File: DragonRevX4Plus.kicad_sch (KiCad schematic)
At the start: 14 parts, among them J14 PWR_LED, J15 PWR_SWITCH, J7 COMPOSITE

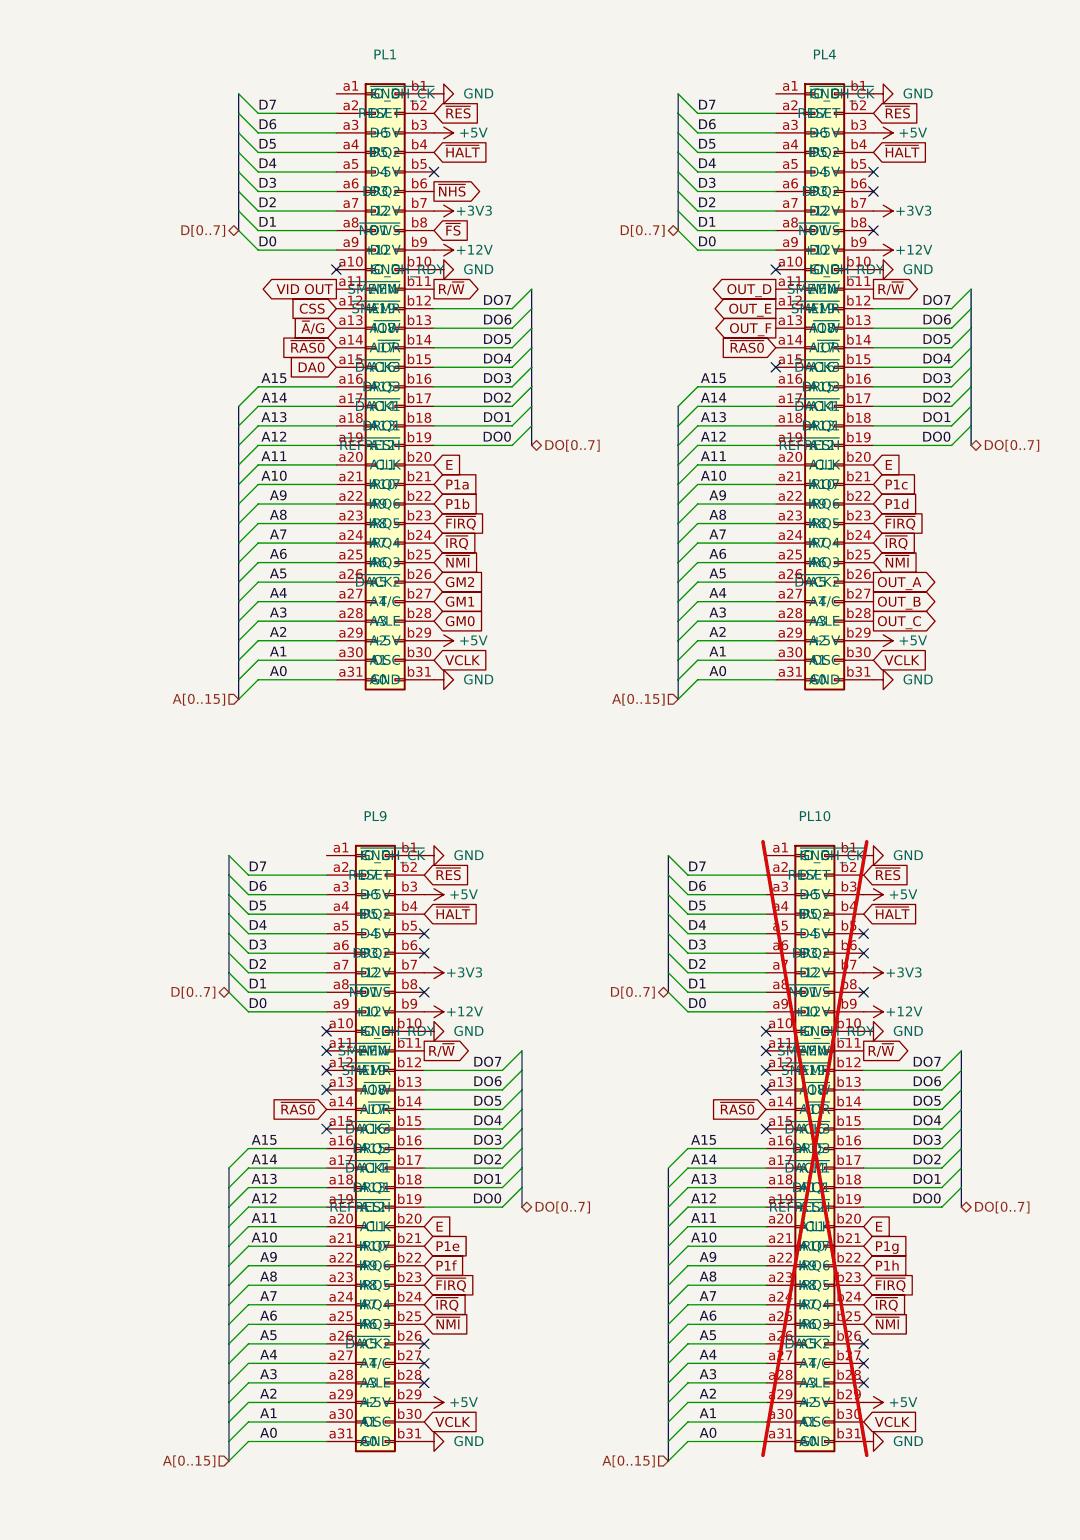
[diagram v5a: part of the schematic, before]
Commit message: Migrate to plugin memory module
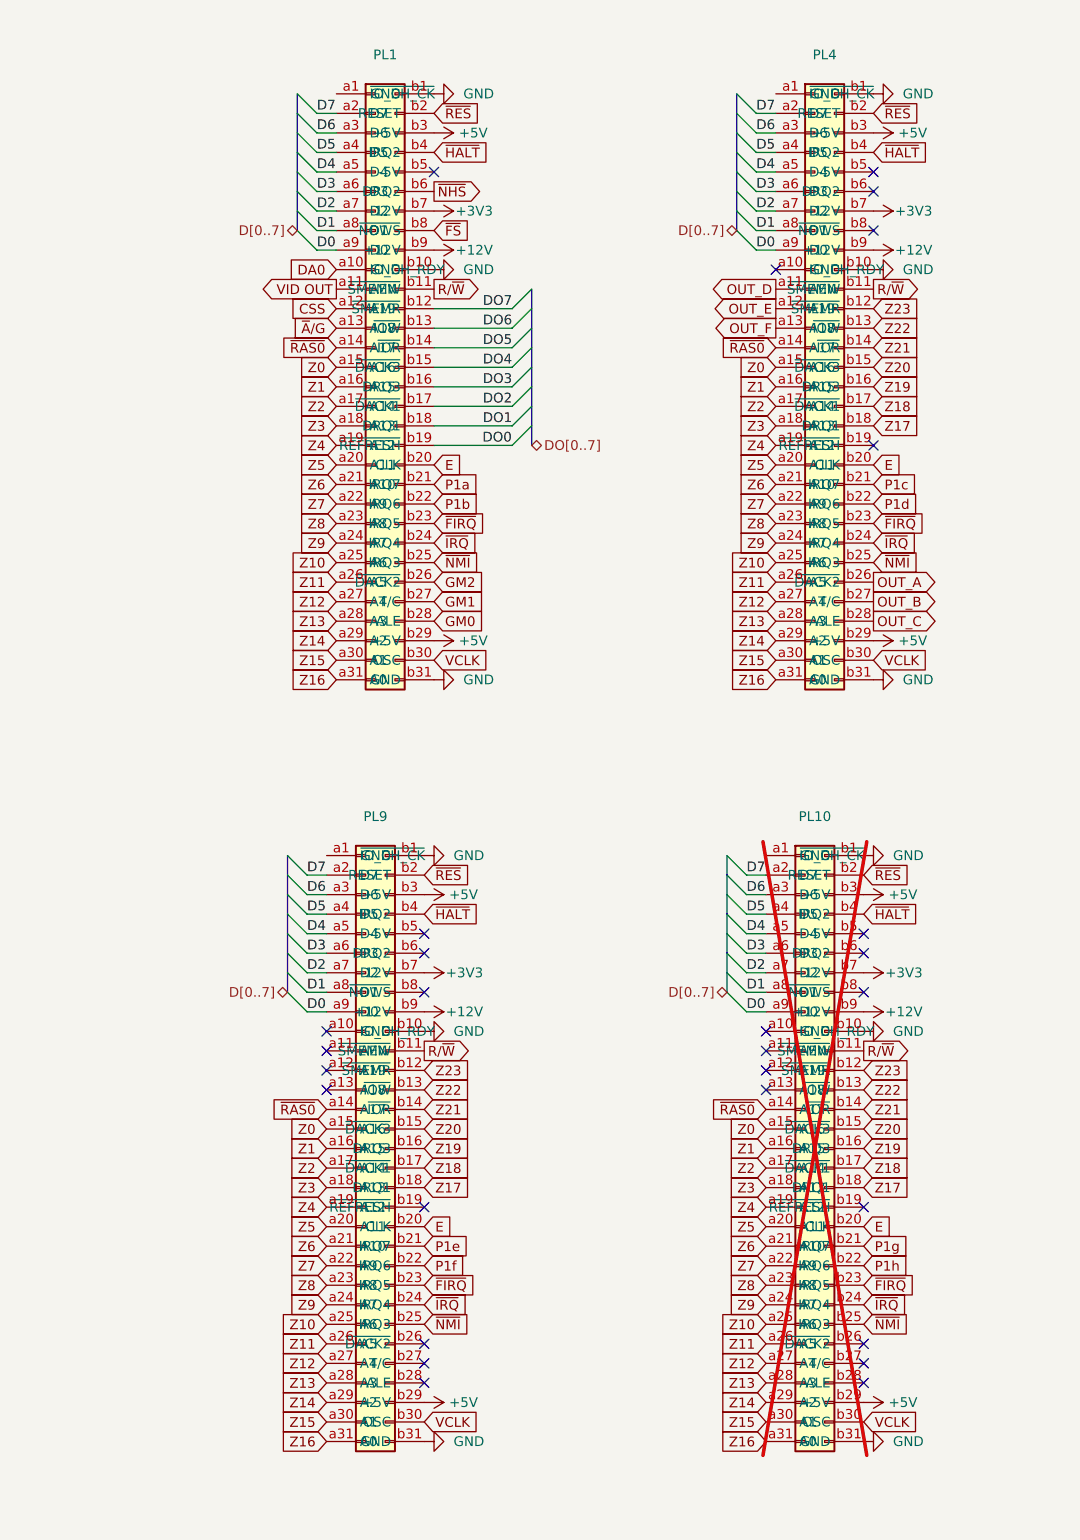
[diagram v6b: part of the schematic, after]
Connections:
- net DA0: now also PL1.a10 (IO_CH_RDY); no longer PL1.a15 (A16)
- net DO0: no longer PL10.b19 (~{REFRESH}), PL4.b19 (~{REFRESH}), PL9.b19 (~{REFRESH})
- net DO1: no longer PL10.b18 (DRQ1), PL4.b18 (DRQ1), PL9.b18 (DRQ1)
- net DO2: no longer PL10.b17 (~{DACK1}), PL4.b17 (~{DACK1}), PL9.b17 (~{DACK1})
- net DO3: no longer PL10.b16 (DRQ3), PL4.b16 (DRQ3), PL9.b16 (DRQ3)
- net DO4: no longer PL10.b15 (~{DACK3}), PL4.b15 (~{DACK3}), PL9.b15 (~{DACK3})
- net DO5: no longer PL10.b14 (~{IOR}), PL4.b14 (~{IOR}), PL9.b14 (~{IOR})
- net DO6: no longer PL10.b13 (~{IOW}), PL4.b13 (~{IOW}), PL9.b13 (~{IOW})
- net DO7: no longer PL10.b12 (~{SMEMR}), PL4.b12 (~{SMEMR}), PL9.b12 (~{SMEMR})
- net Z0: now reaches PL10.a15 (A16)
- net Z0: now also PL1.a15 (A16), PL4.a15 (A16), PL9.a15 (A16)
- net A0 renamed Z16
- net A1 renamed Z15
- net A10 renamed Z6
- net A11 renamed Z5
- net A12 renamed Z4
- net A13 renamed Z3
- net A14 renamed Z2
- net A15 renamed Z1
- net A2 renamed Z14
- net A3 renamed Z13
- net A4 renamed Z12
- net A5 renamed Z11
- net A6 renamed Z10
- net A7 renamed Z9
- net A8 renamed Z8
- net A9 renamed Z7
- new net Z17: PL10.b18 (DRQ1), PL4.b18 (DRQ1), PL9.b18 (DRQ1)
- new net Z18: PL10.b17 (~{DACK1}), PL4.b17 (~{DACK1}), PL9.b17 (~{DACK1})
- new net Z19: PL10.b16 (DRQ3), PL4.b16 (DRQ3), PL9.b16 (DRQ3)
- new net Z20: PL10.b15 (~{DACK3}), PL4.b15 (~{DACK3}), PL9.b15 (~{DACK3})
- new net Z21: PL10.b14 (~{IOR}), PL4.b14 (~{IOR}), PL9.b14 (~{IOR})
- new net Z22: PL10.b13 (~{IOW}), PL4.b13 (~{IOW}), PL9.b13 (~{IOW})
- new net Z23: PL10.b12 (~{SMEMR}), PL4.b12 (~{SMEMR}), PL9.b12 (~{SMEMR})
- no-connect marks 32 -> 31

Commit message: progress routing
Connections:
- net VID OUT: now also PL1.a1 (~{IO_CH_CK}); no longer PL1.a11 (AEN)
- net SOUNDL renamed OUT_L
- net SOUNDR renamed OUT_R
- no-connect marks 31 -> 32
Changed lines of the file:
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@@
 	)
 	(no_connect
+		(at 304.8 50.8)
+	)
+	(no_connect
 		(at 373.38 134.62)
 	)
@@
 		)
 	)
+	(global_label "VID OUT"
+		(shape output)
+		(at 304.8 25.4 180)
+		(fields_autoplaced yes)
+		(effects
+			(font
+				(size 1.27 1.27)
+			)
+			(justify right)
+		)
+		(property "Intersheetrefs" "${INTERSHEET_REFS}"
+			(at 294.2552 25.4 0)
+			(effects
+				(font
+					(size 1.27 1.27)
+				)
+				(justify right)
+				(hide yes)
+			)
+		)
+	)
 	(global_label "Z11"
 		(shape input)
@@
 		)
 	)
+	(global_label "OUT_R"
+		(shape input)
+		(at 78.74 60.96 0)
+		(fields_autoplaced yes)
+		(effects
+			(font
+				(size 1.27 1.27)
+			)
+			(justify left)
+		)
+		(property "Intersheetrefs" "${INTERSHEET_REFS}"
+			(at 87.5914 60.96 0)
+			(effects
+				(font
+					(size 1.27 1.27)
+				)
+				(justify left)
+				(hide yes)
+			)
+		)
+	)
 	(global_label "~{NMI}"
 		(shape input)
@@
 		)
 	)
-	(global_label "VID OUT"
-		(shape output)
-		(at 304.8 50.8 180)
-		(fields_autoplaced yes)
-		(effects
-			(font
-				(size 1.27 1.27)
-			)
-			(justify right)
-		)
-		(property "Intersheetrefs" "${INTERSHEET_REFS}"
-			(at 294.2552 50.8 0)
-			(effects
-				(font
-					(size 1.27 1.27)
-				)
-				(justify right)
-				(hide yes)
-			)
-		)
-	)
 	(global_label "Z10"
 		(shape input)
@@
 		)
 	)
-	(global_label "SOUNDL"
-		(shape input)
-		(at 78.74 58.42 0)
-		(fields_autoplaced yes)
-		(effects
-			(font
-				(size 1.27 1.27)
-			)
-			(justify left)
-		)
-		(property "Intersheetrefs" "${INTERSHEET_REFS}"
-			(at 89.2243 58.42 0)
-			(effects
-				(font
-					(size 1.27 1.27)
-				)
-				(justify left)
-				(hide yes)
-			)
-		)
-	)
 	(global_label "Z2"
 		(shape input)
@@
 		)
 	)
+	(global_label "OUT_L"
+		(shape input)
+		(at 78.74 58.42 0)
+		(fields_autoplaced yes)
+		(effects
+			(font
+				(size 1.27 1.27)
+			)
+			(justify left)
+		)
+		(property "Intersheetrefs" "${INTERSHEET_REFS}"
+			(at 87.3495 58.42 0)
+			(effects
+				(font
+					(size 1.27 1.27)
+				)
+				(justify left)
+				(hide yes)
+			)
+		)
+	)
 	(global_label "Z16"
 		(shape input)
@@
 				(hide yes)
 			)
-		)
-	)
-	(global_label "SOUNDR"
-		(shape input)
-		(at 78.74 60.96 0)
-		(fields_autoplaced yes)
-		(effects
-			(font
-				(size 1.27 1.27)
-			)
-			(justify left)
-		)
-		(property "Intersheetrefs" "${INTERSHEET_REFS}"
-			(at 89.4662 60.96 0)
-			(effects
-				(font
-					(size 1.27 1.27)
-				)
-				(justify left)
-				(hide yes)
-			)

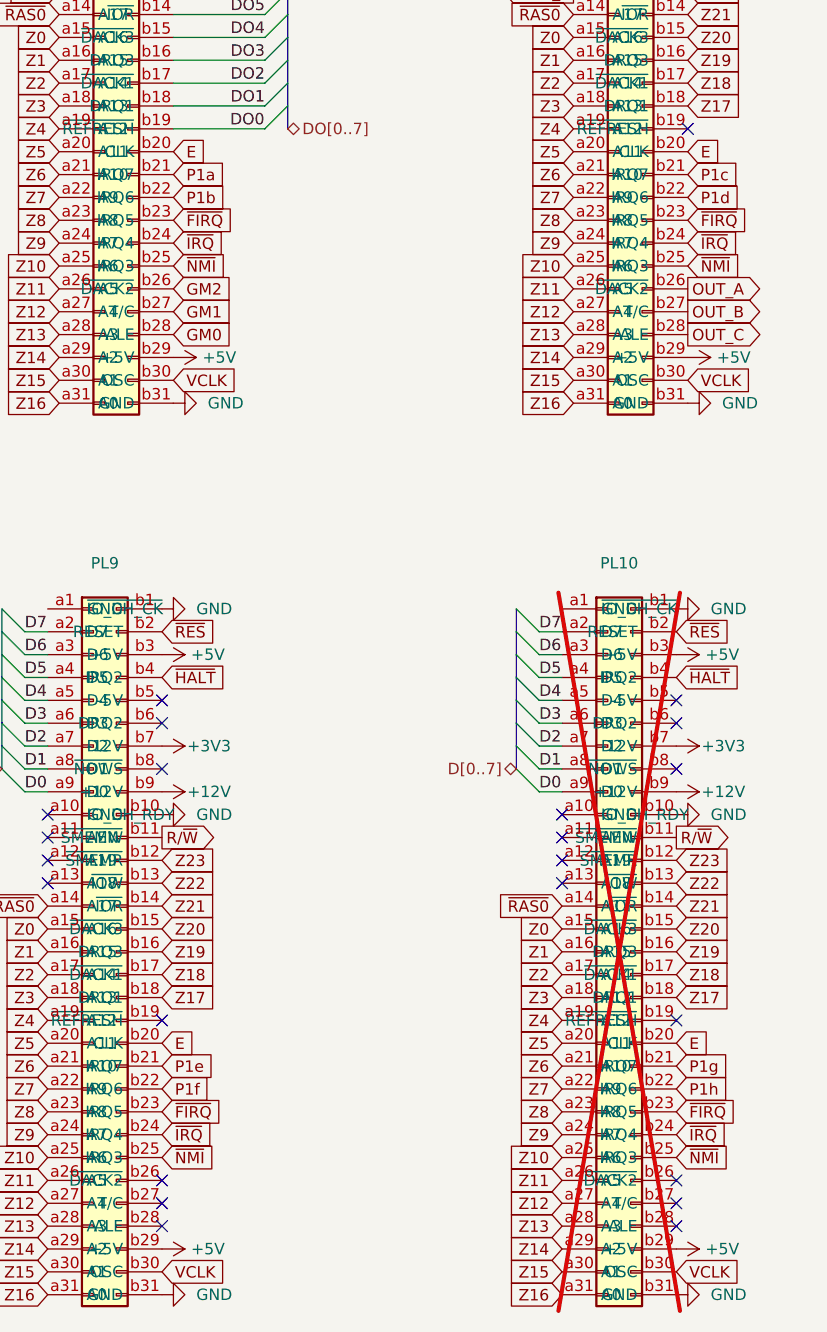
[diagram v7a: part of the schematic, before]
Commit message: migrate to flash rom
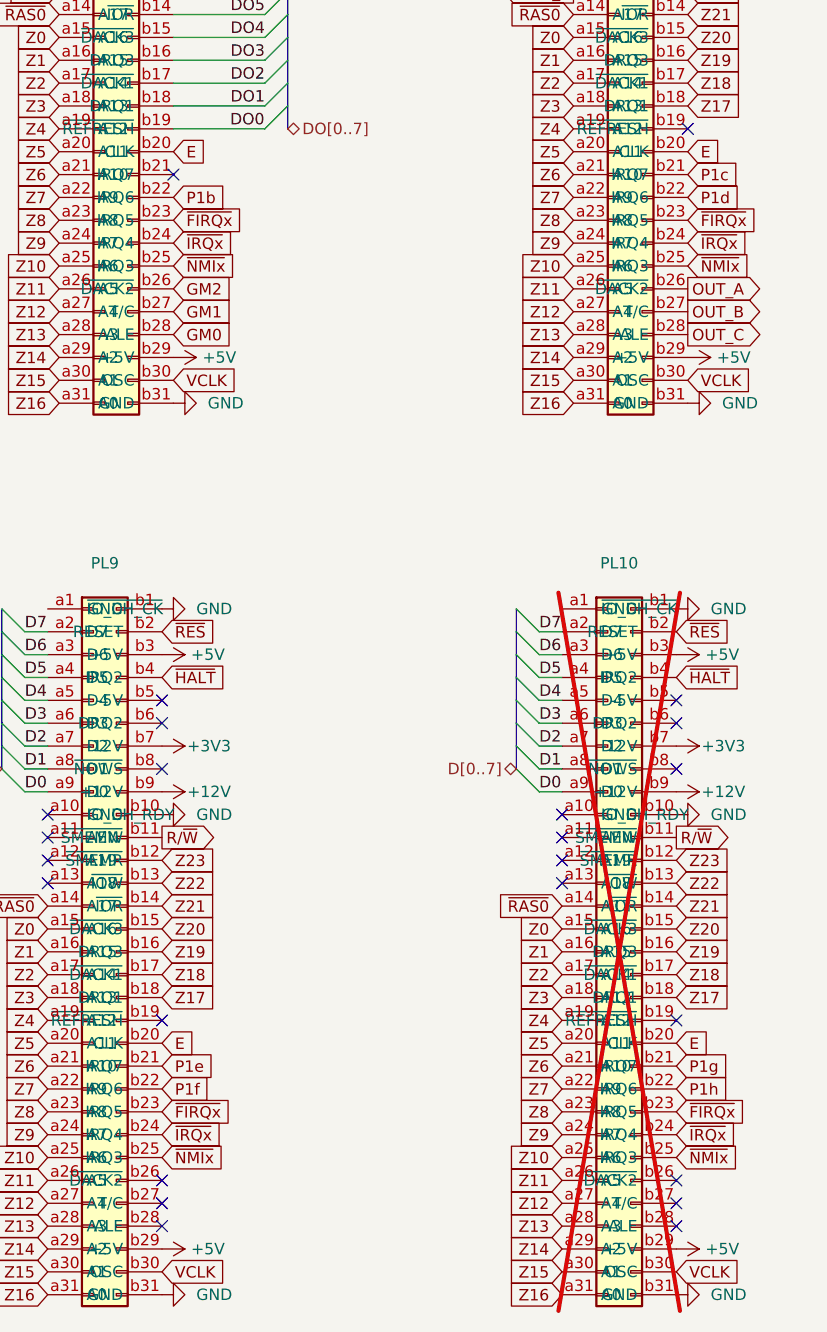
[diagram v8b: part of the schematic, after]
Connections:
- net P1a: no longer names the net of PL1.b21 (IRQ7)
- net ~{FIRQ} renamed ~{FIRQx}
- net ~{IRQ} renamed ~{IRQx}
- net ~{NMI} renamed ~{NMIx}
- no-connect marks 32 -> 33
